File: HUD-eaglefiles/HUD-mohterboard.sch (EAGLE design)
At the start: 24 parts, among them IC1 7805TV, U2 ATMEGA328P_TQFP, Y1 4MHz

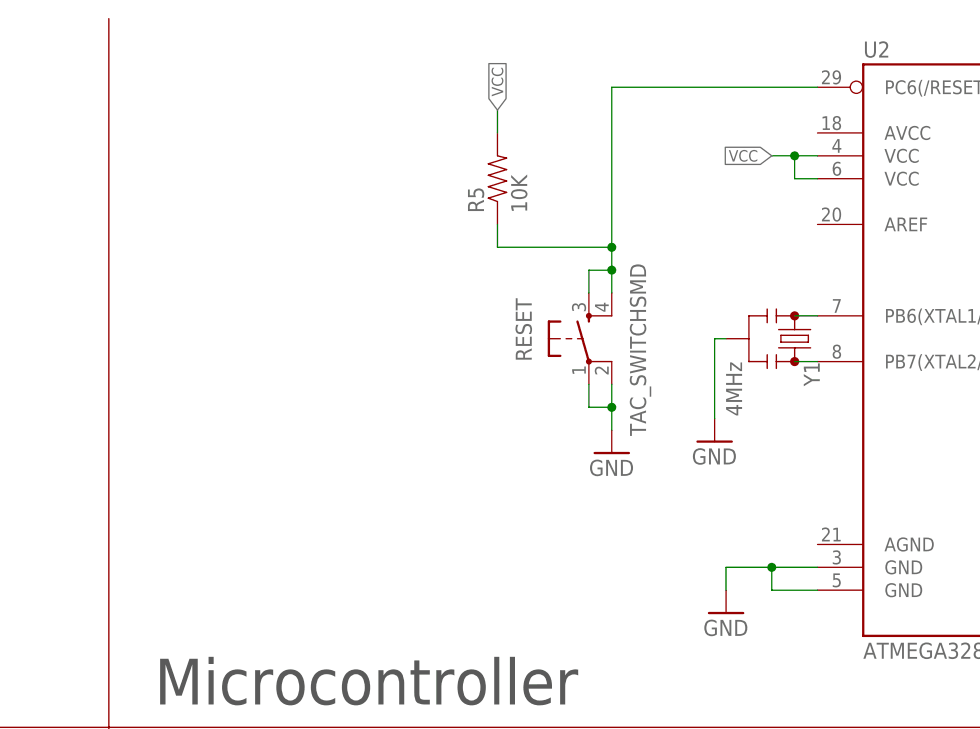
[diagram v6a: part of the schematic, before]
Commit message: new layout for the new schematic
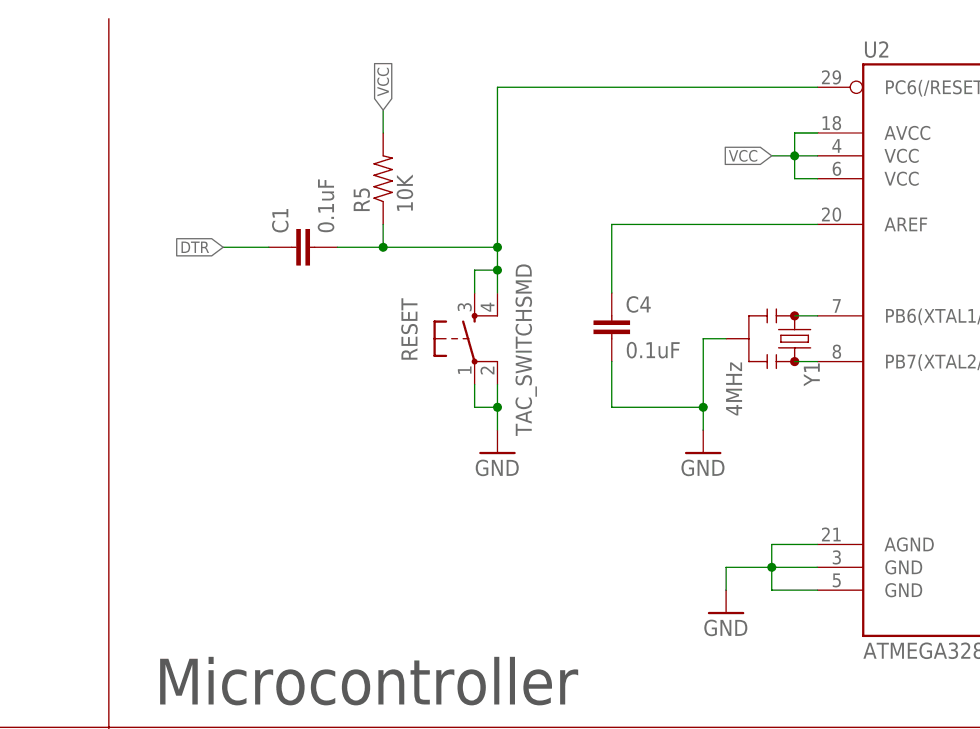
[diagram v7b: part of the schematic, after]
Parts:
- added C1, C4: 0.1uF, SparkFun-Passives:CAP0805
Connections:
- new net N$12: C4.1, U2.AREF
- net DTR: now also C1.1
- net GND: now also C4.2, U2.AGND
- net RESET_WIRE: now also C1.2
- net VCC: now also U2.AVCC
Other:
- moved on the sheet: R5, RESET
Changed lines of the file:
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@@
 <part name="IC1" library="linear" deviceset="78*" device="TV" technology="05"/>
 <part name="GND2" library="SparkFun-Aesthetics" deviceset="GND" device=""/>
+<part name="C1" library="SparkFun-Passives" deviceset="CAP" device="0805" value="0.1uF"/>
+<part name="C4" library="SparkFun-Passives" deviceset="CAP" device="0805" value="0.1uF"/>
 </parts>
 <sheets>
@@
 <attribute name="VALUE" x="193.04" y="187.96" size="1.778" layer="96" font="vector"/>
 </instance>
-<instance part="RESET" gate="S" x="162.56" y="223.52" smashed="yes" rot="R90">
-<attribute name="NAME" x="156.21" y="220.98" size="1.778" layer="95" font="vector" rot="R90"/>
-<attribute name="VALUE" x="168.91" y="212.725" size="1.778" layer="96" font="vector" rot="R90"/>
-</instance>
-<instance part="GND9" gate="1" x="165.1" y="210.82" smashed="yes">
-<attribute name="VALUE" x="162.56" y="208.28" size="1.778" layer="96" font="vector"/>
-</instance>
-<instance part="R5" gate="G$1" x="152.4" y="241.3" smashed="yes" rot="R90">
-<attribute name="NAME" x="150.9014" y="237.49" size="1.778" layer="95" font="vector" rot="R90"/>
-<attribute name="VALUE" x="155.702" y="237.49" size="1.778" layer="96" font="vector" rot="R90"/>
+<instance part="RESET" gate="S" x="149.86" y="223.52" smashed="yes" rot="R90">
+<attribute name="NAME" x="143.51" y="220.98" size="1.778" layer="95" font="vector" rot="R90"/>
+<attribute name="VALUE" x="156.21" y="212.725" size="1.778" layer="96" font="vector" rot="R90"/>
+</instance>
+<instance part="GND9" gate="1" x="152.4" y="210.82" smashed="yes">
+<attribute name="VALUE" x="149.86" y="208.28" size="1.778" layer="96" font="vector"/>
+</instance>
+<instance part="R5" gate="G$1" x="139.7" y="241.3" smashed="yes" rot="R90">
+<attribute name="NAME" x="138.2014" y="237.49" size="1.778" layer="95" font="vector" rot="R90"/>
+<attribute name="VALUE" x="143.002" y="237.49" size="1.778" layer="96" font="vector" rot="R90"/>
 </instance>
 <instance part="DOUT" gate="G$1" x="365.76" y="203.2" smashed="yes" rot="R180">
@@
 </instance>
 <instance part="Y1" gate="G$1" x="185.42" y="223.52" rot="R270"/>
-<instance part="GND1" gate="1" x="176.53" y="212.09"/>
+<instance part="GND1" gate="1" x="175.26" y="210.82"/>
 <instance part="TA_D0" gate="A" x="170.18" y="133.35"/>
 <instance part="TA_D1" gate="A" x="246.38" y="133.35"/>
@@
 <instance part="IC1" gate="A1" x="53.34" y="241.3"/>
 <instance part="GND2" gate="1" x="289.56" y="231.14"/>
+<instance part="C1" gate="G$1" x="132.08" y="233.68" rot="R90"/>
+<instance part="C4" gate="G$1" x="165.1" y="223.52"/>
 </instances>
 <busses>
@@
 <wire x1="177.8" y1="198.12" x2="177.8" y2="195.58" width="0.1524" layer="91"/>
 <junction x="182.88" y="198.12"/>
+<pinref part="U2" gate="U$1" pin="AGND"/>
+<wire x1="187.96" y1="200.66" x2="182.88" y2="200.66" width="0.1524" layer="91"/>
+<wire x1="182.88" y1="200.66" x2="182.88" y2="198.12" width="0.1524" layer="91"/>
 </segment>
 <segment>
 <pinref part="GND9" gate="1" pin="GND"/>
-<wire x1="165.1" y1="213.36" x2="165.1" y2="215.9" width="0.1524" layer="91"/>
+<wire x1="152.4" y1="213.36" x2="152.4" y2="215.9" width="0.1524" layer="91"/>
 <pinref part="RESET" gate="S" pin="2"/>
-<wire x1="165.1" y1="215.9" x2="165.1" y2="218.44" width="0.1524" layer="91"/>
+<wire x1="152.4" y1="215.9" x2="152.4" y2="218.44" width="0.1524" layer="91"/>
 <pinref part="RESET" gate="S" pin="1"/>
-<wire x1="162.56" y1="218.44" x2="162.56" y2="215.9" width="0.1524" layer="91"/>
-<wire x1="162.56" y1="215.9" x2="165.1" y2="215.9" width="0.1524" layer="91"/>
-<junction x="165.1" y="215.9"/>
+<wire x1="149.86" y1="218.44" x2="149.86" y2="215.9" width="0.1524" layer="91"/>
+<wire x1="149.86" y1="215.9" x2="152.4" y2="215.9" width="0.1524" layer="91"/>
+<junction x="152.4" y="215.9"/>
 </segment>
 <segment>
@@
 <segment>
 <pinref part="Y1" gate="G$1" pin="2"/>
-<wire x1="177.8" y1="223.52" x2="176.53" y2="223.52" width="0.1524" layer="91"/>
-<wire x1="176.53" y1="223.52" x2="176.53" y2="214.63" width="0.1524" layer="91"/>
+<wire x1="177.8" y1="223.52" x2="175.26" y2="223.52" width="0.1524" layer="91"/>
+<wire x1="175.26" y1="223.52" x2="175.26" y2="215.9" width="0.1524" layer="91"/>
 <pinref part="GND1" gate="1" pin="GND"/>
+<pinref part="C4" gate="G$1" pin="2"/>
+<wire x1="175.26" y1="215.9" x2="175.26" y2="213.36" width="0.1524" layer="91"/>
+<wire x1="165.1" y1="220.98" x2="165.1" y2="215.9" width="0.1524" layer="91"/>
+<wire x1="165.1" y1="215.9" x2="175.26" y2="215.9" width="0.1524" layer="91"/>
+<junction x="175.26" y="215.9"/>
 </segment>
 <segment>
@@
 <junction x="185.42" y="243.84"/>
 <label x="182.88" y="243.84" size="1.27" layer="95" font="vector" rot="R180" xref="yes"/>
+<pinref part="U2" gate="U$1" pin="AVCC"/>
+<wire x1="187.96" y1="246.38" x2="185.42" y2="246.38" width="0.1524" layer="91"/>
+<wire x1="185.42" y1="246.38" x2="185.42" y2="243.84" width="0.1524" layer="91"/>
 </segment>
 <segment>
 <pinref part="R5" gate="G$1" pin="2"/>
-<wire x1="152.4" y1="246.38" x2="152.4" y2="248.92" width="0.1524" layer="91"/>
-<label x="152.4" y="248.92" size="1.27" layer="95" font="vector" rot="R90" xref="yes"/>
+<wire x1="139.7" y1="246.38" x2="139.7" y2="248.92" width="0.1524" layer="91"/>
+<label x="139.7" y="248.92" size="1.27" layer="95" font="vector" rot="R90" xref="yes"/>
 </segment>
 <segment>
@@
 <segment>
 <pinref part="RESET" gate="S" pin="3"/>
-<wire x1="162.56" y1="228.6" x2="162.56" y2="231.14" width="0.1524" layer="91"/>
-<wire x1="162.56" y1="231.14" x2="165.1" y2="231.14" width="0.1524" layer="91"/>
+<wire x1="149.86" y1="228.6" x2="149.86" y2="231.14" width="0.1524" layer="91"/>
+<wire x1="149.86" y1="231.14" x2="152.4" y2="231.14" width="0.1524" layer="91"/>
 <pinref part="RESET" gate="S" pin="4"/>
-<wire x1="165.1" y1="228.6" x2="165.1" y2="231.14" width="0.1524" layer="91"/>
+<wire x1="152.4" y1="228.6" x2="152.4" y2="231.14" width="0.1524" layer="91"/>
 <pinref part="U2" gate="U$1" pin="PC6(/RESET)"/>
-<wire x1="187.96" y1="251.46" x2="165.1" y2="251.46" width="0.1524" layer="91"/>
-<wire x1="165.1" y1="251.46" x2="165.1" y2="233.68" width="0.1524" layer="91"/>
-<wire x1="165.1" y1="231.14" x2="165.1" y2="233.68" width="0.1524" layer="91"/>
-<junction x="165.1" y="231.14"/>
-<junction x="165.1" y="233.68"/>
+<wire x1="187.96" y1="251.46" x2="152.4" y2="251.46" width="0.1524" layer="91"/>
+<wire x1="152.4" y1="251.46" x2="152.4" y2="233.68" width="0.1524" layer="91"/>
+<wire x1="152.4" y1="231.14" x2="152.4" y2="233.68" width="0.1524" layer="91"/>
+<junction x="152.4" y="231.14"/>
+<junction x="152.4" y="233.68"/>
 <pinref part="R5" gate="G$1" pin="1"/>
-<wire x1="165.1" y1="233.68" x2="152.4" y2="233.68" width="0.1524" layer="91"/>
-<wire x1="152.4" y1="233.68" x2="152.4" y2="236.22" width="0.1524" layer="91"/>
+<wire x1="152.4" y1="233.68" x2="139.7" y2="233.68" width="0.1524" layer="91"/>
+<wire x1="139.7" y1="233.68" x2="139.7" y2="236.22" width="0.1524" layer="91"/>
+<pinref part="C1" gate="G$1" pin="2"/>
+<wire x1="139.7" y1="233.68" x2="134.62" y2="233.68" width="0.1524" layer="91"/>
+<junction x="139.7" y="233.68"/>
 </segment>
 </net>
@@
 <label x="292.1" y="248.92" size="1.27" layer="95" font="vector" rot="R180" xref="yes"/>
 </segment>
-</net>
+<segment>
+<pinref part="C1" gate="G$1" pin="1"/>
+<wire x1="127" y1="233.68" x2="121.92" y2="233.68" width="0.1524" layer="91"/>
+<label x="121.92" y="233.68" size="1.27" layer="95" font="vector" rot="R180" xref="yes"/>
+</segment>
+</net>
+<net name="N$12" class="0">
+<segment>
+<pinref part="U2" gate="U$1" pin="AREF"/>
+<pinref part="C4" gate="G$1" pin="1"/>
+<wire x1="187.96" y1="236.22" x2="165.1" y2="236.22" width="0.1524" layer="91"/>
+<wire x1="165.1" y1="236.22" x2="165.1" y2="228.6" width="0.1524" layer="91"/>
+</segment>
+</net>
